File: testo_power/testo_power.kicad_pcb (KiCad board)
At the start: 2 copper layers, 20 x 30 mm, 10 parts, among them J1 USB_C_Receptacle_PowerOnly_6P, J2 Conn_01x02_Socket, J3 Conn_01x02_Socket, Q2 IRLML6402TRPBF

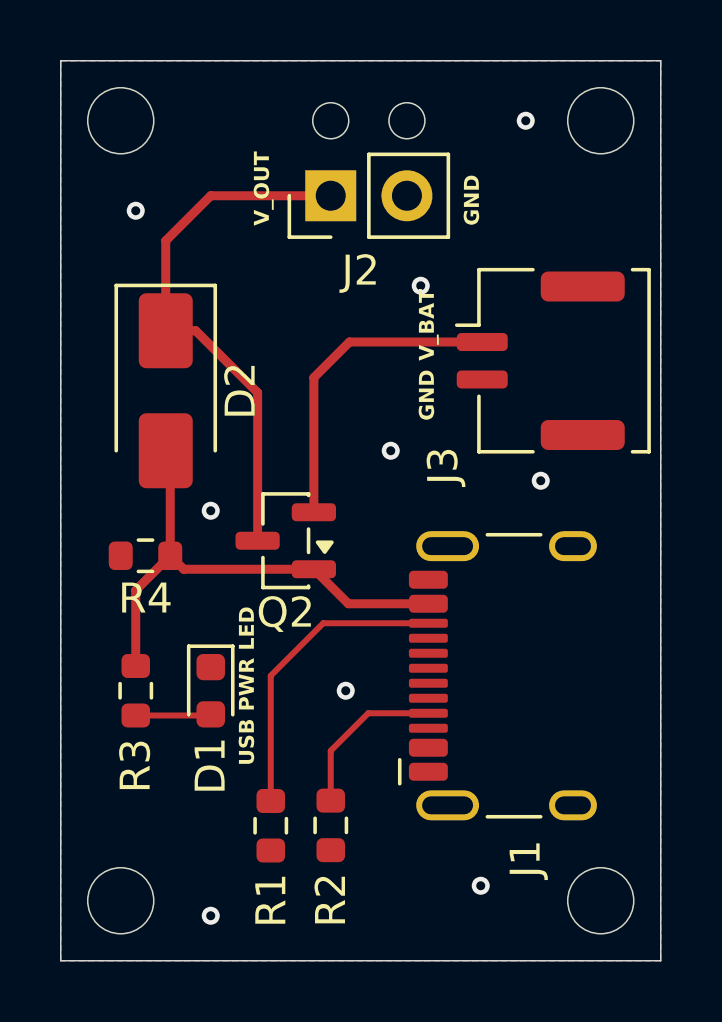
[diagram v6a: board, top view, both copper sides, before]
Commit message: PCB layout with charging and boost circuit
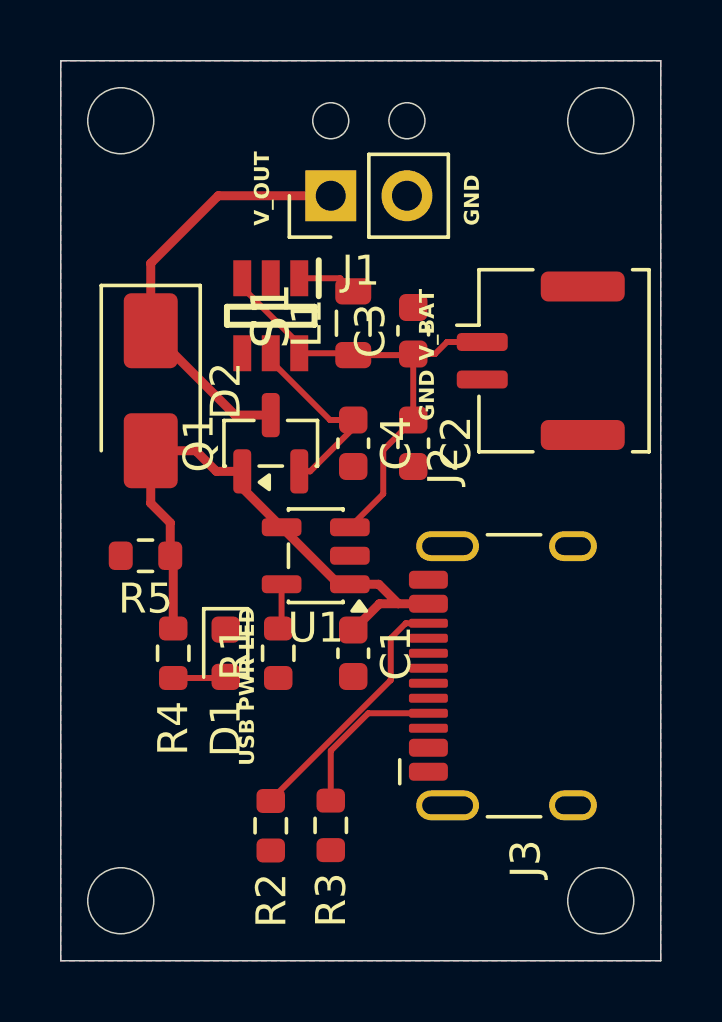
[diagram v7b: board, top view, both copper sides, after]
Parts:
- added C1: 1uF, Capacitor_SMD:C_0603_1608Metric, F.Cu at (109.8, 119.8)
- added C2: 1uF, Capacitor_SMD:C_0603_1608Metric, F.Cu at (111.8, 112.8)
- added C3: 10uF, Capacitor_SMD:C_0603_1608Metric, F.Cu at (111.8, 109.0)
- added C4: 10uF, Capacitor_SMD:C_0603_1608Metric, F.Cu at (109.8, 112.8)
- added L1: 4.7uH, Inductor_SMD:L_0805_2012Metric, F.Cu at (109.8, 108.8)
- added R1: 5k1, Resistor_SMD:R_0603_1608Metric, F.Cu at (107.2, 119.8)
- added S1: SGM6603-5.0YN6G_TR, SamacSys_Parts:SOT95P280X125-6N, F.Cu at (107.0, 108.5)
- added U1: MCP73812, Package_TO_SOT_SMD:SOT-23-5, F.Cu at (108.5, 116.5)
- moved Q1 3.29 mm to (107.0, 112.8), turned to 90 degrees
- moved R4 1.77 mm to (103.8, 119.8)
- moved D1 1.35 mm to (105.5, 119.8)
- moved D2 0.50 mm to (103.0, 111.0)
- renumbered J2 to J1, J3 to J2, J1 to J3, Q2 to Q1, R1 to R2, R2 to R3, R3 to R4, R4 to R5
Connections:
- J2 pad 1: V_BAT -> BOOST_IN
- Q1 pad 2: V_BAT -> BOOST_OUT
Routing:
- net BOOST_IN: track 0.00 -> 16.2 mm
- net V_BAT: track 10.6 -> 0.00 mm
- net BOOST_OUT: track 0.00 -> 6.54 mm
- net V_OUT: track 18.0 -> 14.3 mm
- net V_BUS: track 17.0 -> 20.1 mm
- net Net-(S1-SW): track 0.00 -> 1.98 mm
- net Net-(J3-CC2): track 10.2 -> 8.54 mm
- net Net-(U1-PROG): track 0.00 -> 1.52 mm
- net Net-(D1-A): track 2.52 -> 1.77 mm
- net GND: vias 9 -> 0

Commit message: Improved PCB layout for V1
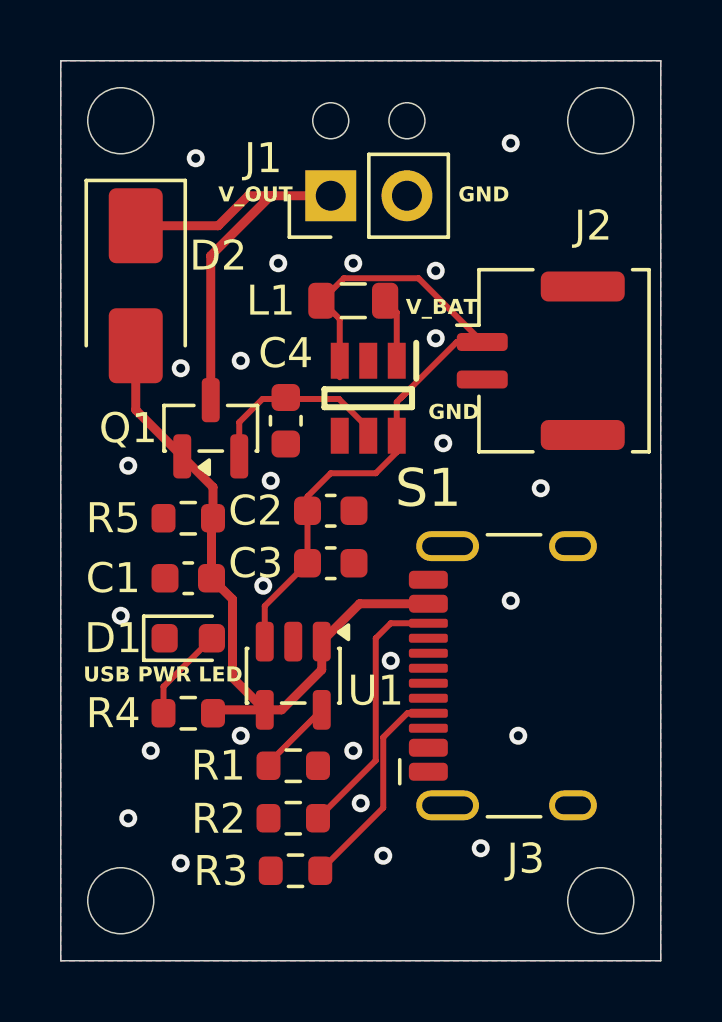
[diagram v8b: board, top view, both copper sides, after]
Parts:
- moved C3 8.22 mm to (109.0, 116.8), turned to 0 degrees
- moved C1 6.04 mm to (104.2, 117.2), turned to 180 degrees
- moved S1 4.26 mm to (110.2, 111.2)
- moved U1 4.07 mm to (107.8, 120.5), turned to -90 degrees
- moved R1 3.78 mm to (107.8, 123.5), turned to 180 degrees
- moved C2 3.55 mm to (109.0, 115.0), turned to 0 degrees
- moved D2 3.54 mm to (102.5, 107.5)
- moved C4 2.37 mm to (107.5, 112.0)
- moved Q1 2.06 mm to (105.0, 112.2)
- moved R4 2.06 mm to (104.2, 121.8), turned to 180 degrees
- moved R3 1.92 mm to (107.8, 127.0), turned to 0 degrees
- moved R5 1.90 mm to (104.2, 115.2)
- moved D1 1.35 mm to (104.2, 119.2), turned to 0 degrees
- moved R2 0.79 mm to (107.8, 125.2), turned to 0 degrees
- moved L1 0.75 mm to (109.8, 108.0), turned to 0 degrees
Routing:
- net BOOST_IN: track 16.2 -> 24.2 mm
- net V_BUS: track 20.1 -> 23.2 mm
- net Net-(J3-CC1): track 5.44 -> 7.15 mm
- net Net-(D1-A): track 1.77 -> 3.17 mm
- net Net-(U1-PROG): track 1.52 -> 2.60 mm
- net GND: vias 0 -> 25
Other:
- board text added: "Testo power selector V1 12/5/2026 Gijs de Vries & Xander Perry"
